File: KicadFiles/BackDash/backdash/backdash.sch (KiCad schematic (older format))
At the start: 3 parts

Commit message: backdash footprints assigned
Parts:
- CAN1: footprint (none) -> TestBaja:CAN_Module
- NANO1: footprint (none) -> TestBaja:arduino_nano
- RTD1: footprint (none) -> TestBaja:RTD
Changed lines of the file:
@@
 EESchema Schematic File Version 4
 LIBS:backdash-cache
-EELAYER 26 0
+EELAYER 28 0
 EELAYER END
 $Descr A4 11693 8268
@@
 F 0 "NANO1" H 1827 2626 50  0000 L CNN
 F 1 "Conn_01x30_Female" H 1827 2535 50  0000 L CNN
-F 2 "" H 1800 2650 50  0001 C CNN
+F 2 "TestBaja:arduino_nano" H 1800 2650 50  0001 C CNN
 F 3 "~" H 1800 2650 50  0001 C CNN
 	1    1800 2650
@@
 F 0 "RTD1" H 2877 1526 50  0000 L CNN
 F 1 "Conn_01x08_Female" H 2877 1435 50  0000 L CNN
-F 2 "" H 2850 1550 50  0001 C CNN
+F 2 "TestBaja:RTD" H 2850 1550 50  0001 C CNN
 F 3 "~" H 2850 1550 50  0001 C CNN
 	1    2850 1550
@@
 F 0 "CAN1" H 3477 2926 50  0000 L CNN
 F 1 "Conn_01x16_Female" H 3477 2835 50  0000 L CNN
-F 2 "" H 3450 2950 50  0001 C CNN
+F 2 "TestBaja:CAN_Module" H 3450 2950 50  0001 C CNN
 F 3 "~" H 3450 2950 50  0001 C CNN
 	1    3450 2950

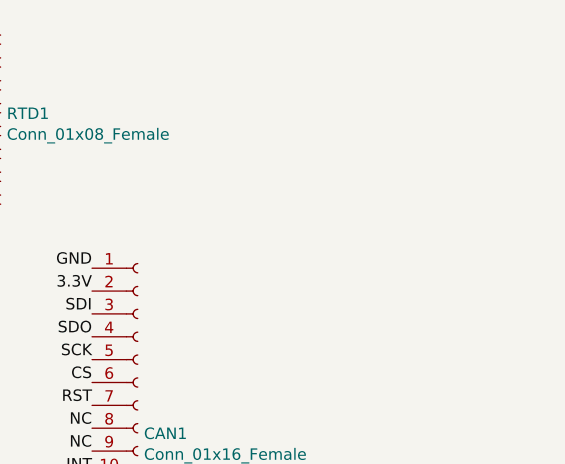
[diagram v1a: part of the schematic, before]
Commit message: backdash footprints assigned
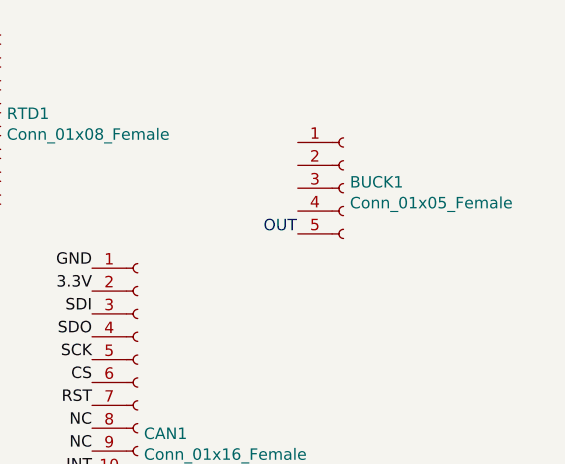
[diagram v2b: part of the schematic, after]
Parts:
- added BUCK1: Conn_01x05_Female, TestBaja:Buck_module, symbol Connector:Conn_01x05_Female
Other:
- note added: "OUT\n"
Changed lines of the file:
@@
 Text Label 3250 3750 2    50   ~ 0
 GND
+$Comp
+L Connector:Conn_01x05_Female BUCK1
+U 1 1 5BDBB2FB
+P 4350 1900
+F 0 "BUCK1" H 4378 1926 50  0000 L CNN
+F 1 "Conn_01x05_Female" H 4378 1835 50  0000 L CNN
+F 2 "TestBaja:Buck_module" H 4350 1900 50  0001 C CNN
+F 3 "~" H 4350 1900 50  0001 C CNN
+	1    4350 1900
+	1    0    0    -1
+$EndComp
+Text Notes 4000 2100 0    50   ~ 0
+OUT\n
 $EndSCHEMATC

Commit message: update backdash
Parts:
- added NANO2, NANO3, NANO4: Conn_01x30_Female, TestBaja:arduino_nano, symbol Connector:Conn_01x30_Female
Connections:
- net 3.3V: now also NANO2.17 (Pin_17), NANO3.17 (Pin_17), NANO4.17 (Pin_17)
- net A0: now also NANO2.19 (Pin_19), NANO3.19 (Pin_19), NANO4.19 (Pin_19)
- net A1: now also NANO2.20 (Pin_20), NANO3.20 (Pin_20), NANO4.20 (Pin_20)
- net A2: now also NANO2.21 (Pin_21), NANO3.21 (Pin_21), NANO4.21 (Pin_21)
- net A3: now also NANO2.22 (Pin_22), NANO3.22 (Pin_22), NANO4.22 (Pin_22)
- net A4: now also NANO2.23 (Pin_23), NANO3.23 (Pin_23), NANO4.23 (Pin_23)
- net A5: now also NANO2.24 (Pin_24), NANO3.24 (Pin_24), NANO4.24 (Pin_24)
- net A6: now also NANO2.25 (Pin_25), NANO3.25 (Pin_25), NANO4.25 (Pin_25)
- net A7: now also NANO2.26 (Pin_26), NANO3.26 (Pin_26), NANO4.26 (Pin_26)
- net D10: now also NANO2.13 (Pin_13), NANO3.13 (Pin_13), NANO4.13 (Pin_13)
- net D11: now also NANO2.14 (Pin_14), NANO3.14 (Pin_14), NANO4.14 (Pin_14)
- net D12: now also NANO2.15 (Pin_15), NANO3.15 (Pin_15), NANO4.15 (Pin_15)
- net D13: now also NANO2.16 (Pin_16), NANO3.16 (Pin_16), NANO4.16 (Pin_16)
- net D2: now also NANO2.5 (Pin_5), NANO3.5 (Pin_5), NANO4.5 (Pin_5)
- net D3: now also NANO2.6 (Pin_6), NANO3.6 (Pin_6), NANO4.6 (Pin_6)
- net D4: now also NANO2.7 (Pin_7), NANO3.7 (Pin_7), NANO4.7 (Pin_7)
- net D5: now also NANO2.8 (Pin_8), NANO3.8 (Pin_8), NANO4.8 (Pin_8)
- net D6: now also NANO2.9 (Pin_9), NANO3.9 (Pin_9), NANO4.9 (Pin_9)
- net D7: now also NANO2.10 (Pin_10), NANO3.10 (Pin_10), NANO4.10 (Pin_10)
- net D8: now also NANO2.11 (Pin_11), NANO3.11 (Pin_11), NANO4.11 (Pin_11)
- net D9: now also NANO2.12 (Pin_12), NANO3.12 (Pin_12), NANO4.12 (Pin_12)
- net GND: now also NANO2.29 (Pin_29), NANO2.4 (Pin_4), NANO3.29 (Pin_29), NANO3.4 (Pin_4), NANO4.29 (Pin_29), NANO4.4 (Pin_4)
- net REF: now also NANO2.18 (Pin_18), NANO3.18 (Pin_18), NANO4.18 (Pin_18)
- net RST: now also NANO2.28 (Pin_28), NANO2.3 (Pin_3), NANO3.28 (Pin_28), NANO3.3 (Pin_3), NANO4.28 (Pin_28), NANO4.3 (Pin_3)
- net RX0: now also NANO2.2 (Pin_2), NANO3.2 (Pin_2), NANO4.2 (Pin_2)
- net TX1: now also NANO2.1 (Pin_1), NANO3.1 (Pin_1), NANO4.1 (Pin_1)
- net VCC: now also NANO2.27 (Pin_27), NANO3.27 (Pin_27), NANO4.27 (Pin_27)
- net VIN: now also NANO2.30 (Pin_30), NANO3.30 (Pin_30), NANO4.30 (Pin_30)
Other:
- moved on the sheet: NANO1

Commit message: need to add in power
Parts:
- removed NANO4: Conn_01x30_Female, TestBaja:arduino_nano, symbol Connector:Conn_01x30_Female
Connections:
- no-connect marks 0 -> 8
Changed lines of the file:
@@
 Text Notes 4000 2100 0    50   ~ 0
 OUT\n
-Text Label 6050 3750 2    50   ~ 0
-A0
-Text Label 6050 3850 2    50   ~ 0
-A1
-Text Label 6050 3950 2    50   ~ 0
-A2
-Text Label 6050 4050 2    50   ~ 0
-A3
-Text Label 6050 4150 2    50   ~ 0
-A4
-Text Label 6050 4250 2    50   ~ 0
-A5
-Text Label 6050 4350 2    50   ~ 0
-A6
-Text Label 6050 4450 2    50   ~ 0
-A7
-Text Label 6050 4550 2    50   ~ 0
-VCC
-Text Label 6050 4650 2    50   ~ 0
-RST
-Text Label 6050 4750 2    50   ~ 0
-GND
-Text Label 6050 4850 2    50   ~ 0
-VIN
-Text Label 6050 3350 2    50   ~ 0
-D12
-Text Label 6050 3250 2    50   ~ 0
-D11
-Text Label 6050 3150 2    50   ~ 0
-D10
-Text Label 6050 3050 2    50   ~ 0
-D9
-Text Label 6050 2950 2    50   ~ 0
-D8
-Text Label 6050 2850 2    50   ~ 0
-D7
-Text Label 6050 2750 2    50   ~ 0
-D6
-Text Label 6050 2650 2    50   ~ 0
-D5
-Text Label 6050 2550 2    50   ~ 0
-D4
-Text Label 6050 2450 2    50   ~ 0
-D3
-Text Label 6050 2350 2    50   ~ 0
-D2
-Text Label 6050 2250 2    50   ~ 0
-GND
-Text Label 6050 2150 2    50   ~ 0
-RST
-Text Label 6050 2050 2    50   ~ 0
-RX0
-$Comp
-L Connector:Conn_01x30_Female NANO4
-U 1 1 5BDBACFE
-P 6250 3350
-F 0 "NANO4" H 6277 3326 50  0000 L CNN
-F 1 "Conn_01x30_Female" H 6277 3235 50  0000 L CNN
-F 2 "TestBaja:arduino_nano" H 6250 3350 50  0001 C CNN
-F 3 "~" H 6250 3350 50  0001 C CNN
-	1    6250 3350
-	1    0    0    -1
-$EndComp
-Text Label 6050 3450 2    50   ~ 0
-D13
-Text Label 6050 3550 2    50   ~ 0
-3.3V
-Text Label 6050 3650 2    50   ~ 0
-REF
-Text Label 6050 1950 2    50   ~ 0
-TX1
 Text Label 1500 6150 2    50   ~ 0
 A0
@@
 Text Label 3250 4450 2    50   ~ 0
 TX1
+NoConn ~ 1700 1100
+NoConn ~ 1700 1200
+NoConn ~ 1700 1300
+NoConn ~ 1550 1300
+NoConn ~ 1550 1200
+NoConn ~ 1550 1100
+NoConn ~ 1750 1400
+NoConn ~ 1750 1500
 $EndSCHEMATC
